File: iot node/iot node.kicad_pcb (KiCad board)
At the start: 2 copper layers, 41 parts, among them J1 Conn_01x04_Female, J2 Conn_01x06_Female, SW1 SW_Push, SW2 SW_Push, SW3 SW_Push, U2 NCP1117-3.3_SOT223, U3 EKMB1305112K, U4 BME680

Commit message: versie 2 sessie2
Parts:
- added U1: ESP32-C3-WROOM-02, esp:ESP32-C3-WROOM-02, F.Cu at (186.9, 138.0)
- added X1: DG3XX-02-5.0, degson:degson-DG306-5.0-02P, F.Cu at (203.4, 130.6)
- moved C7 156.8 mm to (168.7, 106.8)
- moved C8 156.8 mm to (168.7, 103.8)
- moved R4 156.8 mm to (178.3, 103.7)
- moved SW3 156.8 mm to (134.0, 131.5)
- moved TP15 156.8 mm to (164.5, 123.4)
- moved U2 156.8 mm to (148.7, 121.5)
- moved C1 156.8 mm to (126.5, 135.6)
- moved C2 156.8 mm to (156.1, 118.9)
- moved C3 156.8 mm to (131.3, 135.6)
- moved C4 156.8 mm to (146.7, 127.1)
- moved C5 156.8 mm to (136.1, 135.6)
- moved C6 156.8 mm to (141.6, 133.3)
- moved D1 156.8 mm to (173.6, 103.8)
- moved J1 156.8 mm to (131.0, 119.0)
- moved J2 156.8 mm to (126.4, 119.0)
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
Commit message: Eerste PCB
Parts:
- TP1, TP10, TP11, TP12, TP13, TP14, TP15, TP2, TP3, TP4, TP5, TP6, TP7, TP8, TP9: footprint Connector_Pin:Pin_D1.0mm_L10.0mm -> Connector_Pin:Pin_D0.7mm_L6.5mm_W1.8mm_FlatFork
- moved TP10 86.7 mm to (115.2, 51.6)
- moved TP1 79.1 mm to (126.9, 51.5)
- moved U1 79.1 mm to (153.5, 66.3)
- moved R5 77.7 mm to (104.9, 70.5), turned to 180 degrees
- moved TP4 77.6 mm to (99.2, 87.1)
- moved TP6 75.7 mm to (132.3, 51.3)
- moved C3 72.2 mm to (100.0, 70.5)
- moved D1 71.7 mm to (110.1, 70.4)
- moved X1 71.7 mm to (184.5, 61.4), turned to 90 degrees
- moved C2 71.1 mm to (99.9, 75.3)
- moved TP14 65.5 mm to (141.2, 65.6)
- moved TP12 62.3 mm to (141.3, 60.5)
- moved TP2 62.1 mm to (141.3, 73.3)
- moved U3 61.5 mm to (102.8, 58.8)
- moved TP7 61.2 mm to (141.2, 68.2)
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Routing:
- net GND: track 0.00 -> 91.3 mm
- net 3.3: track 0.00 -> 64.8 mm
- net test button: track 0.00 -> 35.5 mm
- net test led: track 0.00 -> 34.6 mm
- net SCL: track 0.00 -> 31.7 mm
- net SDA: track 0.00 -> 16.8 mm
- net Net-(C1-Pad2): track 0.00 -> 7.27 mm
- net buzzer+: track 0.00 -> 4.89 mm
- net Net-(TP2-Pad1): track 0.00 -> 4.81 mm
- net INT PIR: track 0.00 -> 3.97 mm
- net + suply : track 0.00 -> 3.96 mm
- net Net-(D1-Pad1): track 0.00 -> 3.21 mm

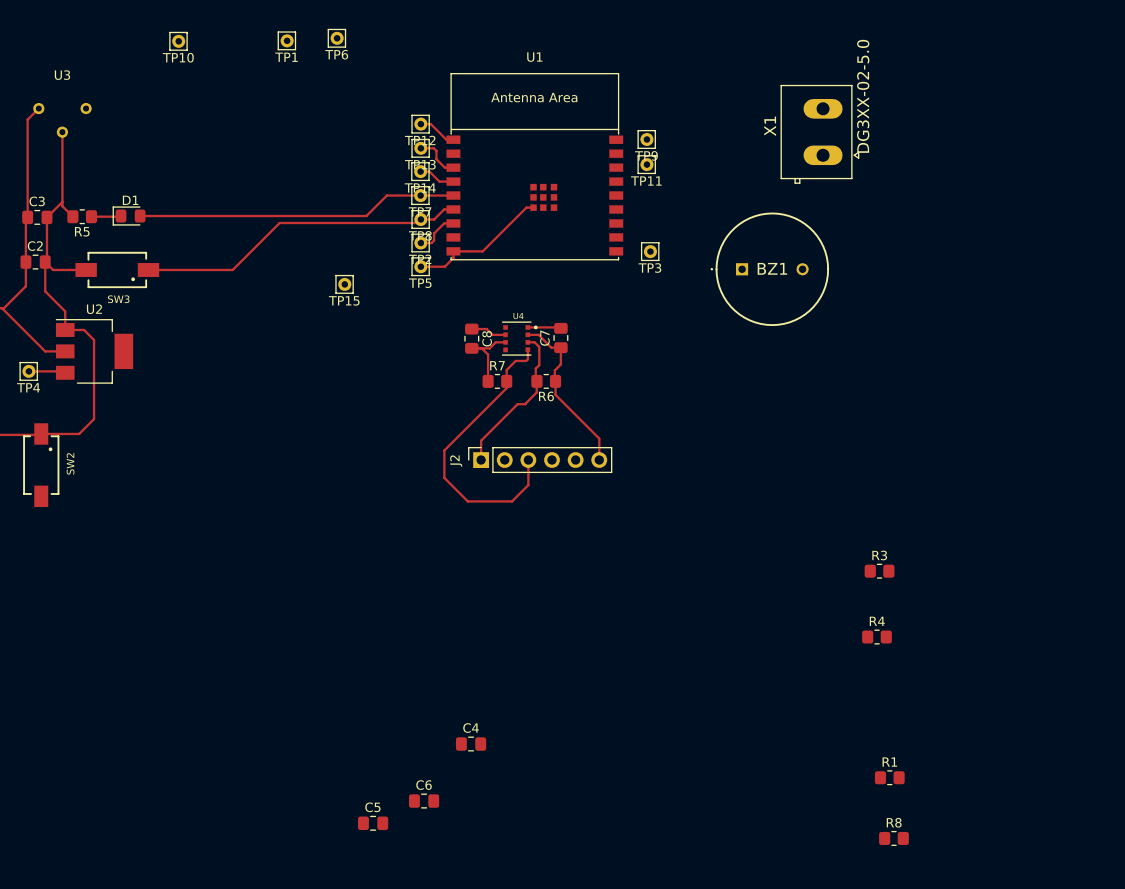
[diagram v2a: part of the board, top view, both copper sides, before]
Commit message: voltage suply adapt
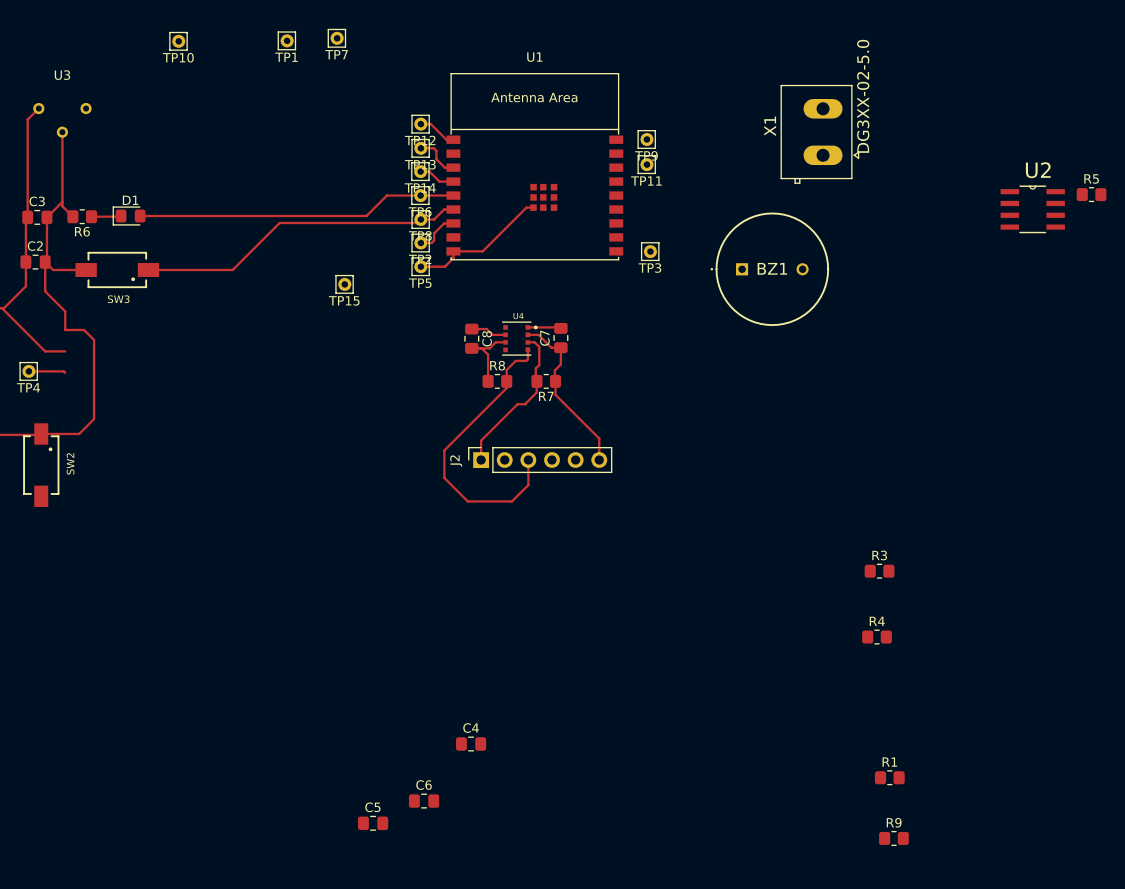
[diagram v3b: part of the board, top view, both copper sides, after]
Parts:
- added R5: 4.7k, Resistor_SMD:R_0805_2012Metric_Pad1.20x1.40mm_HandSolder, F.Cu at (213.4, 68.1)
- C4: value 10u -> 2.2u
- C5: value 10u -> 4.7u
- U2: value NCP1117-3.3_SOT223 -> LP2989IMX-3.3/NOPB; footprint Package_TO_SOT_SMD:SOT-223-3_TabPin2 -> LP2989IMX-3:SOIC127P600X175-8N
- moved U2 102.0 mm to (207.0, 69.7)
- renumbered R5 to R6, R6 to R7, R7 to R8, R8 to R9, TP7 to TP6, TP6 to TP7
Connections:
- U2 pad 1: GND -> unconnected-(U2-Pad1)
- U2 pad 2: 3.3 -> unconnected-(U2-Pad2)
- U2 pad 3: + suply  -> GND

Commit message: pcb
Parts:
- removed TP12: TestPoint, Connector_Pin:Pin_D0.7mm_L6.5mm_W1.8mm_FlatFork
- added  : MountingHole_2.1mm, MountingHole:MountingHole_2.1mm, F.Cu at (159.9, 100.2)
- added  : MountingHole_2.1mm, MountingHole:MountingHole_2.1mm, F.Cu at (91.2, 100.2)
- added REF: MountingHole_2.1mm, MountingHole:MountingHole_2.1mm, F.Cu at (118.3, 143.2)
- BZ1, J1, J2, U3: moved to B.Cu
- R9: value 10k -> 1meg
- moved R5 114.0 mm to (110.1, 116.4), turned to 90 degrees
- moved U2 103.8 mm to (111.3, 109.8)
- moved X1 103.8 mm to (93.7, 111.5), turned to -90 degrees
- moved R3 88.6 mm to (102.1, 112.8), turned to 180 degrees
- moved R4 88.5 mm to (102.1, 108.0)
- moved R9 85.8 mm to (106.5, 142.0), turned to 180 degrees
- moved BZ1 83.8 mm to (116.0, 134.8), turned to 180 degrees
- moved TP10 82.7 mm to (147.9, 127.6), turned to -90 degrees
- moved TP7 81.7 mm to (139.0, 132.7)
- moved D1 81.2 mm to (157.2, 136.4), turned to 180 degrees
- moved R6 73.8 mm to (157.1, 122.6)
- moved U3 73.7 mm to (95.9, 132.2), turned to 90 degrees
- moved TP1 72.5 mm to (107.2, 121.3)
- moved SW3 72.4 mm to (157.1, 130.1), turned to 90 degrees
- moved TP13 69.4 mm to (110.2, 125.2)
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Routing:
- net GND: track 91.3 -> 336.9 mm, vias 0 -> 4
- net 3.3: track 64.8 -> 220.0 mm, vias 0 -> 2
- net batterij level: track 0.00 -> 65.3 mm, vias 0 -> 2
- net INT PIR: track 3.97 -> 56.7 mm, vias 0 -> 2
- net Net-(SW2-Pad2): track 0.00 -> 39.0 mm
- net test button: track 35.5 -> 71.2 mm, vias 0 -> 2
- net + suply : track 3.96 -> 36.3 mm
- net Net-(C1-Pad2): track 7.27 -> 39.3 mm
- net buzzer+: track 4.89 -> 35.2 mm, vias 0 -> 3
- net TX: track 0.00 -> 29.8 mm, vias 0 -> 2
- net SDA: track 16.8 -> 42.2 mm, vias 0 -> 1
- net test led: track 34.6 -> 56.6 mm, vias 0 -> 2
- net RX: track 0.00 -> 16.9 mm, vias 0 -> 3
- net Net-(D1-Pad1): track 3.21 -> 16.1 mm
- net SCL: track 31.7 -> 41.0 mm, vias 0 -> 1
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- added copper zone on B.Cu, net GND
- added copper zone on F.Cu, net GND
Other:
- board outline added: 74.8 x 49.8 mm
- board text added: "BOOT"
- board text added: "EN"
- board text added: "GND"
- board text added: "IoT nodes: Team clean air"
- board text added: "RX"
- board text added: "SCL"
- board text added: "SDA"
- board text added: "TX"
- board text added: "V+"
